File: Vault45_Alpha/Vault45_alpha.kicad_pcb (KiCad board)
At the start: 2 copper layers, 247.7 x 76.8 mm, 139 parts, among them J1 AVR-ISP-6, SW1 SW_PUSH, SW2 SW_PUSH, SW3 RotaryEncoder_Switch, U1 SRV05-4, U2 ATmega32U4-M, X1 Crystal_GND24_Small

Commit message: updated pcb layout to address interference with plate mounting hardware and added custom plate files
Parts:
- removed K_SPACE27, K_SPACE39, K_SPACE41, K_SPACE46, K_SPACE50, K_SPACE51, K_SPACE54, K_SPACE55: KEYSW, MX_Only:MXOnly-1U-NoLED
- removed K_SPACE33, K_SPACE48: KEYSW, MX_Only:MXOnly-1.25U-NoLED
- removed K_SPACE49, K_SPACE56: KEYSW, MX_Only:MXOnly-1.75U-NoLED
- K_SPACE40, K_SPACE47: footprint MX_Only:MXOnly-1.25U-NoLED -> MX_Only:MXOnly-1U-NoLED
- K_SPACE52, K_SPACE53: footprint MX_Only:MXOnly-1.5U-NoLED -> MX_Only:MXOnly-2U-ReversedStabilizers-NoLED
- moved D_SPACE45 24.4 mm to (206.0, 98.4)
- moved D_SPACE41 12.6 mm to (83.9, 98.4)
- moved D_SPACE44 10.7 mm to (185.1, 98.4)
- moved D_SPACE27 9.53 mm to (43.5, 79.4)
- moved D_SPACE40 7.85 mm to (62.5, 98.4)
- moved K_SPACE58 5.36 mm to (102.4, 97.6)
- moved K_SPACE52 5.36 mm to (131.0, 97.6)
- moved K_SPACE57 5.36 mm to (81.0, 97.6)
- moved D_SPACE39 4.76 mm to (262.5, 79.4)
- moved K_SPACE60 4.17 mm to (219.1, 97.6)
- moved K_SPACE59 4.17 mm to (197.6, 97.6)
- moved K_SPACE53 4.17 mm to (169.1, 97.6)
- moved D_SPACE43 3.57 mm to (147.0, 98.4)
- moved K_SPACE40 2.98 mm to (59.5, 97.6)
- moved D_SPACE42 2.50 mm to (113.1, 98.4)
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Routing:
- net col4: track 112.8 -> 136.8 mm
- net Net-(D_SPACE46-A): track 15.5 -> 4.40 mm
- net row3: track 232.9 -> 242.6 mm
- net Net-(D_SPACE41-A): track 13.4 -> 3.79 mm
- net Net-(D_SPACE44-A): track 8.35 -> 17.7 mm
- net Net-(D_SPACE45-A): track 19.1 -> 9.93 mm
- net col10: track 143.2 -> 134.7 mm
- net col2: track 152.0 -> 143.5 mm
- net Net-(D_SPACE39-A): track 10.7 -> 3.79 mm
- net Net-(D_SPACE27-A): track 10.7 -> 3.79 mm
- net Net-(D_SPACE43-A): track 8.35 -> 15.3 mm
- net col12: track 161.8 -> 155.1 mm
- net col3: track 132.1 -> 126.4 mm
- net col9: track 125.2 -> 120.2 mm
- net row2: track 255.6 -> 260.6 mm
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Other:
- board size 247.7 x 76.8 mm -> 247.7 x 76.2 mm
- board text removed: "1.25u"
- board text removed: "1.5u"
- board text removed: "1u"

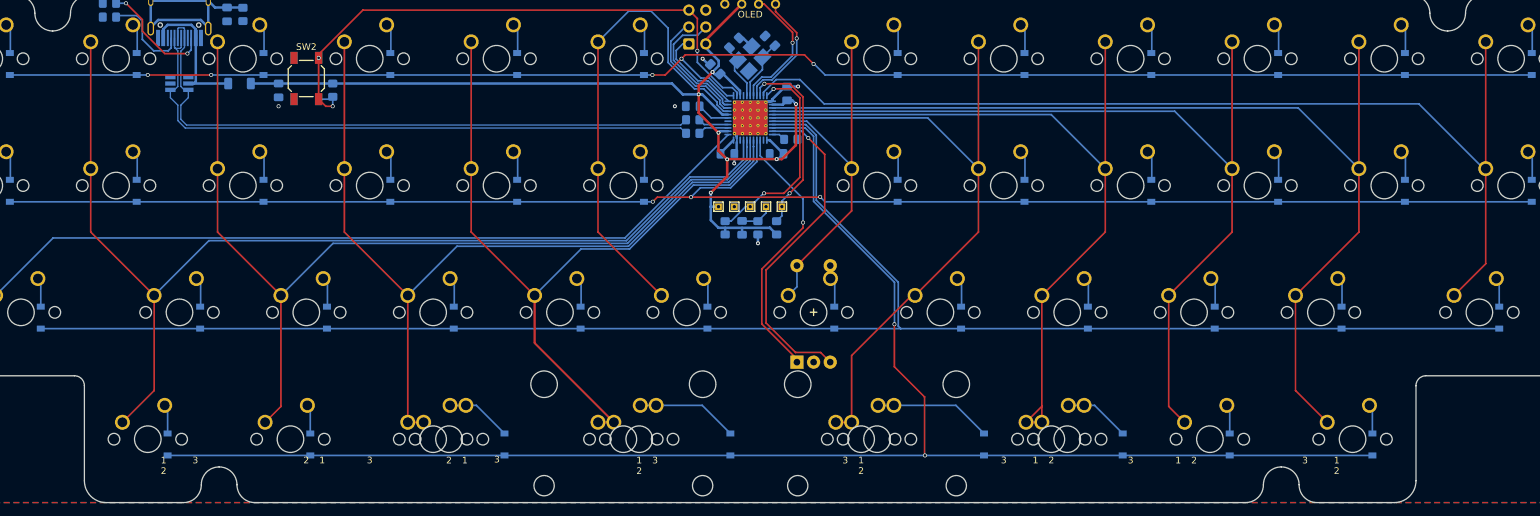
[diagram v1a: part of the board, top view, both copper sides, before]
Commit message: Added bottom row options to Vault 45 Alpha PCB and updated fabrication files.
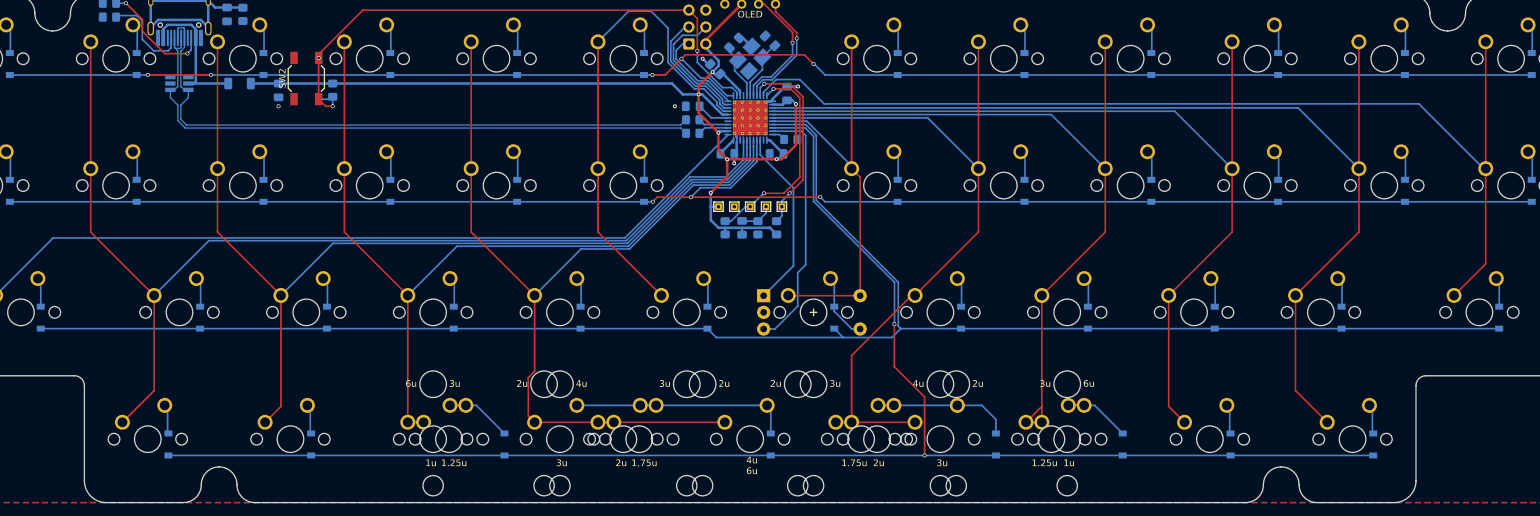
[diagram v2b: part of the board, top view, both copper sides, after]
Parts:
- added K_SPACE52: KEYSW, MX_Only:MXOnly-3U-ReversedStabilizers-NoLED, F.Cu at (121.4, 97.6)
- added K_SPACE53: KEYSW, MX_Only:MXOnly-3U-ReversedStabilizers-NoLED, F.Cu at (178.6, 97.6)
- added K_SPACE54: KEYSW, MX_Only:MXOnly-4U-ReversedStabilizers-NoLED, F.Cu at (150.0, 97.6)
- moved SW3 7.88 mm to (159.5, 78.6), turned to 0 degrees
- moved D_SPACE43 6.08 mm to (153.1, 98.4)
- moved D_SPACE44 1.79 mm to (186.9, 98.4)
- moved D_SPACE47 0.12 mm to (243.6, 98.4)
- moved D_SPACE40 0.12 mm to (62.6, 98.4)
- moved D_SPACE41 0.12 mm to (84.1, 98.4)
- moved D_SPACE46 0.12 mm to (222.2, 98.4)
- renumbered K_SPACE20 to K_SPACE39, K_SPACE57 to K_SPACE41, K_SPACE60 to K_SPACE46, K_SPACE58 to K_SPACE48, K_SPACE52 to K_SPACE49, K_SPACE53 to K_SPACE50, K_SPACE59 to K_SPACE51
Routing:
- net Net-(D_SPACE43-A): track 15.3 -> 32.2 mm
- net encA: track 40.3 -> 27.3 mm, vias 1 -> 0
- net encB: track 50.3 -> 37.9 mm, vias 1 -> 0
- net col8: track 101.3 -> 113.2 mm
- net col7: track 56.7 -> 64.1 mm
- net Net-(D_SPACE34-A): track 3.59 -> 9.36 mm
- net Net-(D_SPACE44-A): track 17.7 -> 20.7 mm
- net row2: track 260.6 -> 263.6 mm
- net GND: track 16.9 -> 15.6 mm, vias 6 -> 5
- net Net-(D_SPACE47-A): track 4.40 -> 3.79 mm
- net Net-(D_SPACE46-A): track 4.40 -> 3.79 mm
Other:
- board text added: "1.25u"
- board text added: "1.75u"
- board text added: "1u"
- board text added: "2u"
- board text added: "3u"
- board text added: "4u"
- board text added: "4u 6u"
- board text added: "6u"
- board text removed: "1"
- board text removed: "2"
- board text removed: "3"
